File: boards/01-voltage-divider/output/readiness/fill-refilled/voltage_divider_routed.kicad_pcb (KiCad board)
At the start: 2 copper layers, 30 x 25 mm, 4 parts, among them J1 IN, J2 OUT

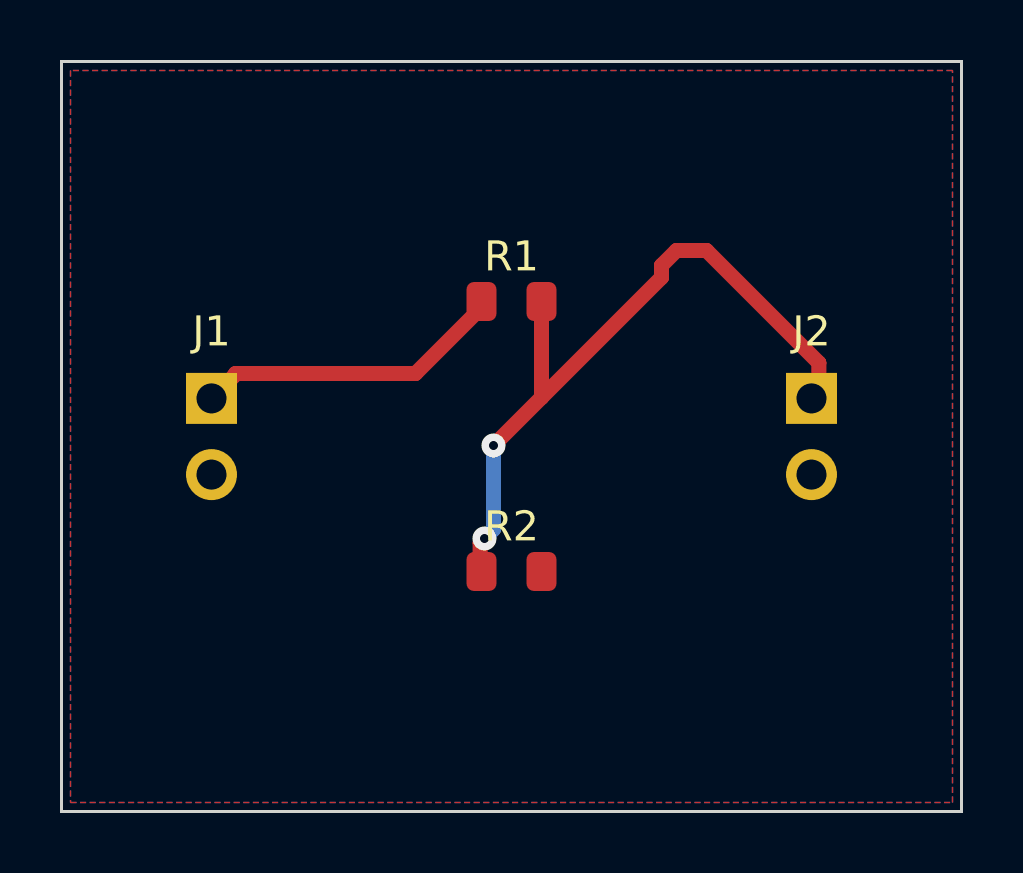
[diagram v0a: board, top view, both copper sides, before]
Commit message: fix(board01): generator emits 3D model blocks; regenerate routed PCB and release package (#6354)
generate_design.py now writes the four (model ...) blocks as literal text,
so a fresh run is byte-identical to the committed voltage_divider.kicad_pcb.
Routed PCB regenerated with the current router (14 segments, 4 vias; was
21/2), package_release.py rerun. Adds a board-01 design-capture
reproducibility test.

Closes #6354

Co-Authored-By: Claude Sonnet 5.5 <noreply@anthropic.com>
Loom-Story: rjwalters/kicad-tools#6354
Loom-Trace-Id: 937fd562e889e1f31b030577b8aaad38
Loom-Build: 0.19.1157 3e3ff8aa9b674281336009ed9b92693dd038f9e9 clean
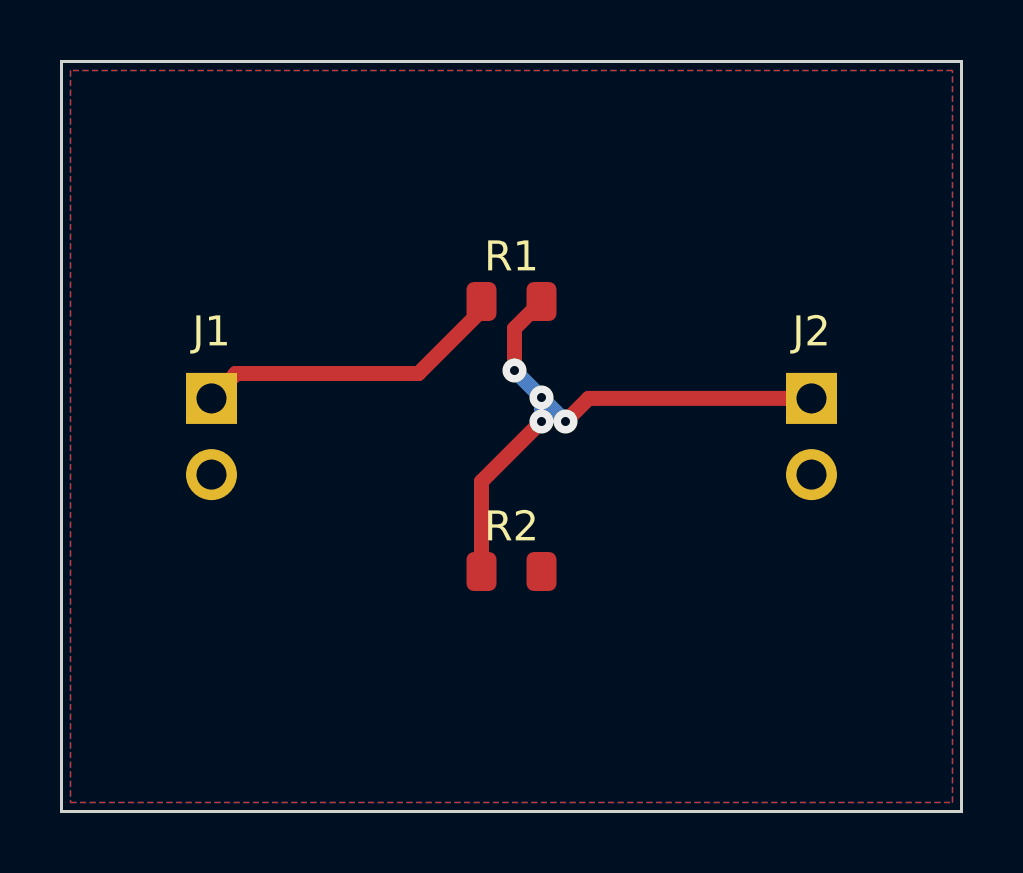
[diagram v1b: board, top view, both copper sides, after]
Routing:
- net VOUT: track 24.2 -> 20.2 mm, vias 2 -> 4
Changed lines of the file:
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@@
 	(segment
 		(start 139.3 85.4)
-		(end 145.3 85.4)
+		(end 145.4 85.4)
+		(width 0.5)
+		(layer "F.Cu")
+		(net 1)
+	)
+	(segment
+		(start 139.3 85.43)
+		(end 139.3 85.4)
+		(width 0.5)
+		(layer "F.Cu")
+		(net 1)
+	)
+	(segment
+		(start 147.5 83.3)
+		(end 147.5 83)
 		(width 0.5)
 		(layer "F.Cu")
@@
 	)
 	(segment
-		(start 139.3 85.43)
-		(end 139.3 85.4)
+		(start 145.4 85.4)
+		(end 147.5 83.3)
 		(width 0.5)
 		(layer "F.Cu")
@@
 	)
 	(segment
-		(start 145.3 85.4)
-		(end 147.5 83.2)
-		(width 0.5)
-		(layer "F.Cu")
-		(net 1)
-	)
-	(segment
-		(start 147.5 83.2)
-		(end 147.5 83)
-		(width 0.5)
-		(layer "F.Cu")
-		(net 1)
-	)
-	(segment
-		(start 153.5 82.2)
-		(end 153.5 81.8)
+		(start 150.3 87)
+		(end 151.07 86.23)
 		(width 0.5)
 		(layer "F.Cu")
@@
 	)
 	(segment
-		(start 158.7464 85.7536)
-		(end 158.5 86)
+		(start 149.5 83)
+		(end 148.6 83.9)
 		(width 0.5)
 		(layer "F.Cu")
@@
 	)
 	(segment
-		(start 147.4536 91.7536)
-		(end 147.5 91.8)
-		(width 0.5)
-		(layer "F.Cu")
-		(net 2)
-	)
-	(segment
-		(start 158.5 86)
+		(start 151.07 86.23)
 		(end 158.5 86.23)
 		(width 0.5)
@@
 	)
 	(segment
-		(start 147.5 91.8)
+		(start 149.5 87)
+		(end 147.5 89)
+		(width 0.5)
+		(layer "F.Cu")
+		(net 2)
+	)
+	(segment
+		(start 148.6 83.9)
+		(end 148.6 85.3)
+		(width 0.5)
+		(layer "F.Cu")
+		(net 2)
+	)
+	(segment
+		(start 147.5 89)
 		(end 147.5 92)
 		(width 0.5)
@@
 		(net 2)
 	)
-	(segment
-		(start 149.5 86.2)
-		(end 153.5 82.2)
-		(width 0.5)
-		(layer "F.Cu")
-		(net 2)
-	)
-	(segment
-		(start 147.4536 91.0464)
-		(end 147.4536 91.7536)
-		(width 0.5)
-		(layer "F.Cu")
-		(net 2)
-	)
-	(segment
-		(start 149.5 83)
-		(end 149.5 86.2)
-		(width 0.5)
-		(layer "F.Cu")
-		(net 2)
-	)
-	(segment
-		(start 149.5 86.2)
-		(end 147.9 87.8)
-		(width 0.5)
-		(layer "F.Cu")
-		(net 2)
-	)
-	(segment
-		(start 147.6 90.9)
-		(end 147.4536 91.0464)
-		(width 0.5)
-		(layer "F.Cu")
-		(net 2)
-	)
-	(segment
-		(start 154 81.3)
-		(end 155 81.3)
-		(width 0.5)
-		(layer "F.Cu")
-		(net 2)
-	)
-	(segment
-		(start 155 81.3)
-		(end 158.7464 85.0464)
-		(width 0.5)
-		(layer "F.Cu")
-		(net 2)
-	)
-	(segment
-		(start 158.7464 85.0464)
-		(end 158.7464 85.7536)
-		(width 0.5)
-		(layer "F.Cu")
-		(net 2)
-	)
-	(segment
-		(start 153.5 81.8)
-		(end 154 81.3)
-		(width 0.5)
-		(layer "F.Cu")
-		(net 2)
-	)
 	(via
-		(at 147.6 90.9)
+		(at 149.5 86.2)
 		(size 0.8)
 		(drill 0.3)
@@
 	)
 	(via
-		(at 147.9 87.8)
+		(at 148.6 85.3)
+		(size 0.8)
+		(drill 0.3)
+		(layers "F.Cu" "B.Cu")
+		(net 2)
+	)
+	(via
+		(at 150.3 87)
+		(size 0.8)
+		(drill 0.3)
+		(layers "F.Cu" "B.Cu")
+		(net 2)
+	)
+	(via
+		(at 149.5 87)
 		(size 0.8)
 		(drill 0.3)
@@
 	)
 	(segment
-		(start 147.9 87.8)
-		(end 147.9 90.6)
+		(start 149.5 86.2)
+		(end 149.5 87)
 		(width 0.5)
 		(layer "B.Cu")
@@
 	)
 	(segment
-		(start 147.9 90.6)
-		(end 147.6 90.9)
+		(start 149.5 86.2)
+		(end 150.3 87)
 		(width 0.5)
 		(layer "B.Cu")
+		(net 2)
+	)
+	(segment
+		(start 148.6 85.3)
+		(end 149.5 86.2)
+		(width 0.5)
+		(layer "B.Cu")

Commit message: fix(router): drop single-layer junction vias in cleanup_artifacts (#6596)
Board 01's VOUT carried a through via at (149.5, 86.2) bonding three B.Cu
segments and no F.Cu copper, which KiCad reports as via_dangling.

Origin (traced by dumping net 2's routes before cleanup): neither of the
curated hypotheses. build_rsmt synthesises the Steiner branch point as a
virtual pad with the first terminal's layer (F.Cu). The RSMT edge that
ends at that point reached it on B.Cu, so A* added a via to land on the
pad's layer; both branches leaving the point then started on B.Cu. The
via was present in the raw route before any optimiser ran.

Fix: a new connectivity-checked Step 5 in Autorouter.cleanup_artifacts
(_remove_single_layer_vias). A via is nominated when its net has known
pads and its same-net segments/vias overlap it on fewer than two layers
(terminal_connectivity.single_layer_via_indices). Micro, in-pad,
pad-touching, pour-net and same-net-zone vias are never nominated, and
preserved input copper counts as bonding copper. Each candidate is
removed only if the net's layer-aware copper component count
(copper_component_count) does not rise; otherwise it is restored. The
new stat is single_layer_vias_removed.

Board 01 regenerated in kicad/kicad:10.0 (10.0.6) with generate_design.py
and package_release.py: the only copper change is the removed via; the
readiness gate is READY; kicad-cli pcb drc --refill-zones no longer
reports via_dangling.

Closes #6596

Co-Authored-By: Claude Opus 5.5 (1M context) <noreply@anthropic.com>
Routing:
- net VOUT: vias 4 -> 3
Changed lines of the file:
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@@
-	)
-	(via
-		(at 149.5 86.2)
-		(size 0.8)
-		(drill 0.3)
-		(layers "F.Cu" "B.Cu")
-		(net 2)
 	)
 	(via
